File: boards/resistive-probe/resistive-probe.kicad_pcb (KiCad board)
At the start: 2 copper layers, 60 x 9 mm, 6 parts, among them P1 MMCX, P2 SOLDERPAD, P3 SOLDERPAD

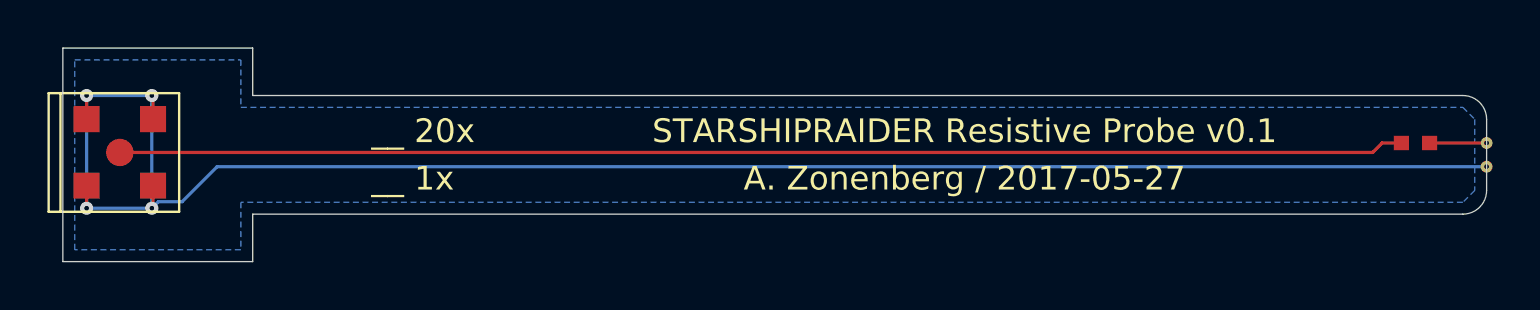
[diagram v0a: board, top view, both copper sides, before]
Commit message: Final layout of probe board ready for fab. Added teardropping and changed export settings
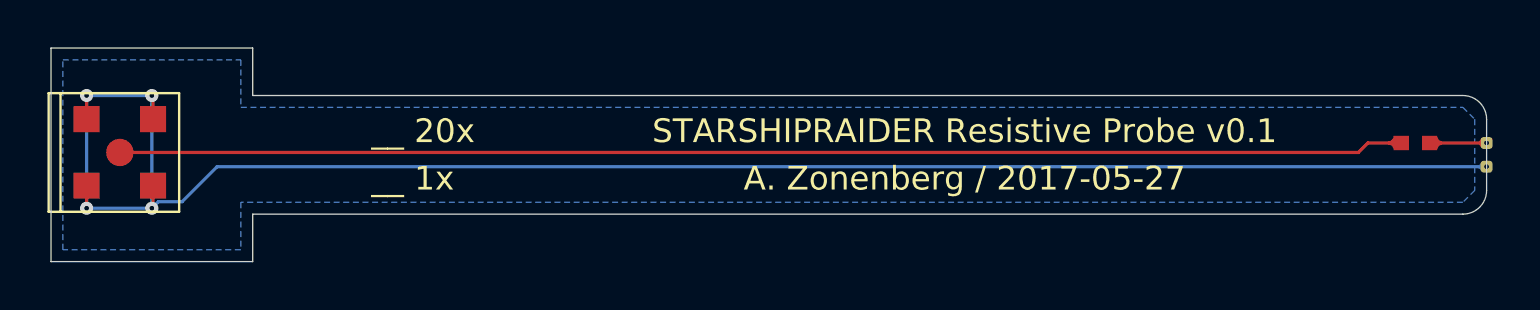
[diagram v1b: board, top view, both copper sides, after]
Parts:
- added G***: TEARDROP_03, azonenberg_pcb:TEARDROP_03, B.Cu at (146.7, 51.1)
- added G***: TEARDROP_03, azonenberg_pcb:TEARDROP_03, B.Cu at (146.7, 50.9)
- added G***: TEARDROP_03, azonenberg_pcb:TEARDROP_03, F.Cu at (146.7, 50.1)
- added G***: TEARDROP_03, azonenberg_pcb:TEARDROP_03, F.Cu at (146.7, 49.9)
- added G***: TEARDROP_02, azonenberg_pcb:TEARDROP_02, F.Cu at (145.0, 50.2)
- added G***: TEARDROP_02, azonenberg_pcb:TEARDROP_02, F.Cu at (145.0, 49.8)
- added G***: TEARDROP_02, azonenberg_pcb:TEARDROP_02, F.Cu at (143.0, 50.2)
- added G***: TEARDROP_02, azonenberg_pcb:TEARDROP_02, F.Cu at (143.0, 49.8)
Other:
- board size 60 x 9 mm -> 60.5 x 9 mm
